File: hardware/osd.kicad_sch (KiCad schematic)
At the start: 17 parts, among them U18 SN74LVC1G3157DTBR, U19 TLV9061IDPWR, U20 TLV3201AIDBVR

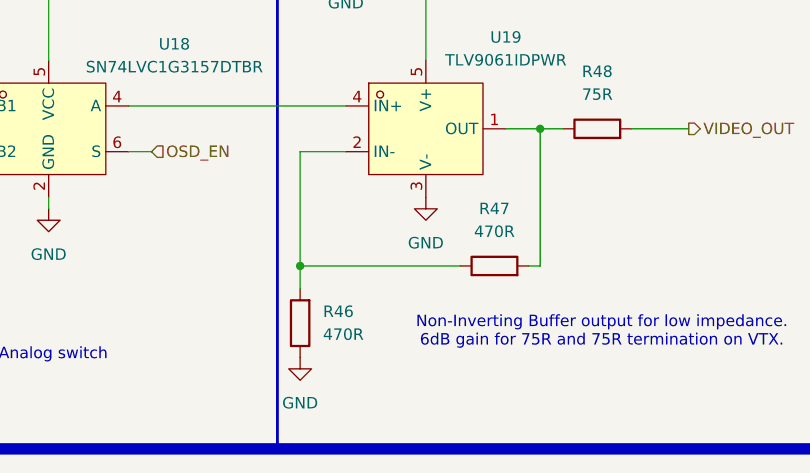
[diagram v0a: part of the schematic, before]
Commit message: LED resistors
Also reduced the amount of different resistors for cheaper assembly
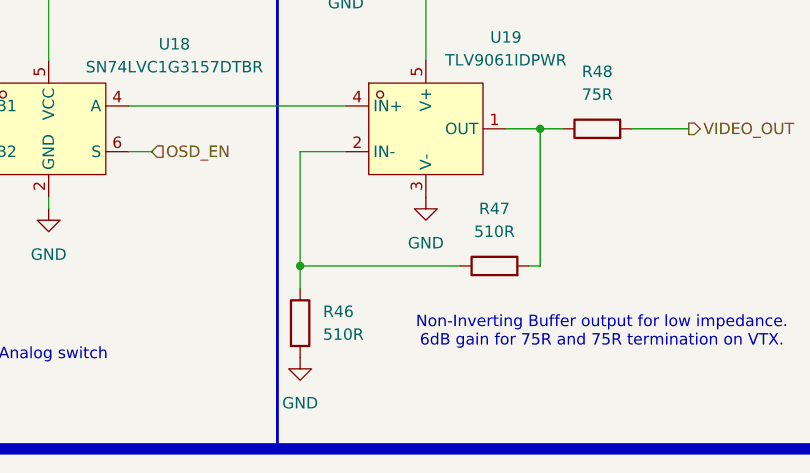
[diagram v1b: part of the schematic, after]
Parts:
- R46, R47: value 470R -> 510R; LCSC C473464 -> C57784; MPN 0201WMF4700TEE -> (none); Manufacturer UNI-ROYAL -> (none)
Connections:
- net GND: now also R46.2; no longer R46.1
- net at R47.1, U19.2 (IN-): now also R46.1; no longer R46.2
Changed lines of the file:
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@@
+	)
+	(symbol
+		(lib_id "Device:R")
+		(at 177.8 186.69 0)
+		(unit 1)
+		(body_style 1)
+		(exclude_from_sim no)
+		(in_bom yes)
+		(on_board yes)
+		(in_pos_files yes)
+		(dnp no)
+		(fields_autoplaced yes)
+		(property "Reference" "R46"
+			(at 180.34 185.4199 0)
+			(show_name no)
+			(do_not_autoplace no)
+			(effects
+				(font
+					(size 1.27 1.27)
+				)
+				(justify left)
+			)
+		)
+		(property "Value" "510R"
+			(at 180.34 187.9599 0)
+			(show_name no)
+			(do_not_autoplace no)
+			(effects
+				(font
+					(size 1.27 1.27)
+				)
+				(justify left)
+			)
+		)
+		(property "Footprint" "Resistor_SMD:R_0201_0603Metric"
+			(at 176.022 186.69 90)
+			(hide yes)
+			(show_name no)
+			(do_not_autoplace no)
+			(effects
+				(font
+					(size 1.27 1.27)
+				)
+			)
+		)
+		(property "Datasheet" ""
+			(at 177.8 186.69 0)
+			(hide yes)
+			(show_name no)
+			(do_not_autoplace no)
+			(effects
+				(font
+					(size 1.27 1.27)
+				)
+			)
+		)
+		(property "Description" "Resistor"
+			(at 177.8 186.69 0)
+			(hide yes)
+			(show_name no)
+			(do_not_autoplace no)
+			(effects
+				(font
+					(size 1.27 1.27)
+				)
+			)
+		)
+		(property "LCSC" "C57784"
+			(at 177.8 186.69 0)
+			(hide yes)
+			(show_name no)
+			(do_not_autoplace no)
+			(effects
+				(font
+					(size 1.27 1.27)
+				)
+			)
+		)
+		(property "MPN" ""
+			(at -74.93 82.55 0)
+			(hide yes)
+			(show_name no)
+			(do_not_autoplace no)
+			(effects
+				(font
+					(size 1.27 1.27)
+				)
+			)
+		)
+		(property "Manufacturer" ""
+			(at -74.93 82.55 0)
+			(hide yes)
+			(show_name no)
+			(do_not_autoplace no)
+			(effects
+				(font
+					(size 1.27 1.27)
+				)
+			)
+		)
+		(pin "1"
+		)
+		(pin "2"
+		)
+		(instances
+			(project "OpenFC"
+				(path "/fb88b6f9-ee39-4640-a9d4-04a17ceeac64/cd9508c6-33b2-4092-8e87-ecfbafcee27b"
+					(reference "R46")
+					(unit 1)
+				)
+			)
+		)
 	)
 	(symbol
@@
 	)
 	(symbol
-		(lib_id "Device:R")
-		(at 177.8 186.69 180)
-		(unit 1)
-		(body_style 1)
-		(exclude_from_sim no)
-		(in_bom yes)
-		(on_board yes)
-		(in_pos_files yes)
-		(dnp no)
-		(fields_autoplaced yes)
-		(property "Reference" "R46"
-			(at 180.34 185.4199 0)
-			(show_name no)
-			(do_not_autoplace no)
-			(effects
-				(font
-					(size 1.27 1.27)
-				)
-				(justify right)
-			)
-		)
-		(property "Value" "470R"
-			(at 180.34 187.9599 0)
-			(show_name no)
-			(do_not_autoplace no)
-			(effects
-				(font
-					(size 1.27 1.27)
-				)
-				(justify right)
-			)
-		)
-		(property "Footprint" "Resistor_SMD:R_0201_0603Metric"
-			(at 179.578 186.69 90)
-			(hide yes)
-			(show_name no)
-			(do_not_autoplace no)
-			(effects
-				(font
-					(size 1.27 1.27)
-				)
-			)
-		)
-		(property "Datasheet" ""
-			(at 177.8 186.69 0)
-			(hide yes)
-			(show_name no)
-			(do_not_autoplace no)
-			(effects
-				(font
-					(size 1.27 1.27)
-				)
-			)
-		)
-		(property "Description" "Resistor"
-			(at 177.8 186.69 0)
-			(hide yes)
-			(show_name no)
-			(do_not_autoplace no)
-			(effects
-				(font
-					(size 1.27 1.27)
-				)
-			)
-		)
-		(property "LCSC" "C473464"
-			(at 177.8 186.69 0)
-			(hide yes)
-			(show_name no)
-			(do_not_autoplace no)
-			(effects
-				(font
-					(size 1.27 1.27)
-				)
-			)
-		)
-		(property "MPN" "0201WMF4700TEE"
-			(at 0 0 0)
-			(hide yes)
-			(show_name no)
-			(do_not_autoplace no)
-			(effects
-				(font
-					(size 1.27 1.27)
-				)
-			)
-		)
-		(property "Manufacturer" "UNI-ROYAL"
-			(at 0 0 0)
-			(hide yes)
-			(show_name no)
-			(do_not_autoplace no)
-			(effects
-				(font
-					(size 1.27 1.27)
-				)
-			)
-		)
-		(pin "1"
-		)
-		(pin "2"
-		)
-		(instances
-			(project "OpenFC"
-				(path "/fb88b6f9-ee39-4640-a9d4-04a17ceeac64/cd9508c6-33b2-4092-8e87-ecfbafcee27b"
-					(reference "R46")
-					(unit 1)
-				)
-			)
-		)
-	)
-	(symbol
 		(lib_id "power:GND")
 		(at 168.91 119.38 0)
@@
 	)
 	(symbol
+		(lib_id "Device:R")
+		(at 199.39 180.34 90)
+		(unit 1)
+		(body_style 1)
+		(exclude_from_sim no)
+		(in_bom yes)
+		(on_board yes)
+		(in_pos_files yes)
+		(dnp no)
+		(fields_autoplaced yes)
+		(property "Reference" "R47"
+			(at 199.39 173.99 90)
+			(show_name no)
+			(do_not_autoplace no)
+			(effects
+				(font
+					(size 1.27 1.27)
+				)
+			)
+		)
+		(property "Value" "510R"
+			(at 199.39 176.53 90)
+			(show_name no)
+			(do_not_autoplace no)
+			(effects
+				(font
+					(size 1.27 1.27)
+				)
+			)
+		)
+		(property "Footprint" "Resistor_SMD:R_0201_0603Metric"
+			(at 199.39 182.118 90)
+			(hide yes)
+			(show_name no)
+			(do_not_autoplace no)
+			(effects
+				(font
+					(size 1.27 1.27)
+				)
+			)
+		)
+		(property "Datasheet" ""
+			(at 199.39 180.34 0)
+			(hide yes)
+			(show_name no)
+			(do_not_autoplace no)
+			(effects
+				(font
+					(size 1.27 1.27)
+				)
+			)
+		)
+		(property "Description" "Resistor"
+			(at 199.39 180.34 0)
+			(hide yes)
+			(show_name no)
+			(do_not_autoplace no)
+			(effects
+				(font
+					(size 1.27 1.27)
+				)
+			)
+		)
+		(property "LCSC" "C57784"
+			(at 199.39 180.34 0)
+			(hide yes)
+			(show_name no)
+			(do_not_autoplace no)
+			(effects
+				(font
+					(size 1.27 1.27)
+				)
+			)
+		)
+		(property "MPN" ""
+			(at 95.25 433.07 0)
+			(hide yes)
+			(show_name no)
+			(do_not_autoplace no)
+			(effects
+				(font
+					(size 1.27 1.27)
+				)
+			)
+		)
+		(property "Manufacturer" ""
+			(at 95.25 433.07 0)
+			(hide yes)
+			(show_name no)
+			(do_not_autoplace no)
+			(effects
+				(font
+					(size 1.27 1.27)
+				)
+			)
+		)
+		(pin "1"
+		)
+		(pin "2"
+		)
+		(instances
+			(project "OpenFC"
+				(path "/fb88b6f9-ee39-4640-a9d4-04a17ceeac64/cd9508c6-33b2-4092-8e87-ecfbafcee27b"
+					(reference "R47")
+					(unit 1)
+				)
+			)
+		)
+	)
+	(symbol
 		(lib_id "power:GND")
 		(at 191.77 172.72 0)
@@
 					(unit 1)
 				)
-			)
-		)
-	)
-	(symbol
-		(lib_id "Device:R")
-		(at 199.39 180.34 90)
-		(unit 1)
-		(body_style 1)
-		(exclude_from_sim no)
-		(in_bom yes)
-		(on_board yes)
-		(in_pos_files yes)
-		(dnp no)
-		(fields_autoplaced yes)
-		(property "Reference" "R47"
-			(at 199.39 173.99 90)
-			(show_name no)
-			(do_not_autoplace no)
-			(effects
-				(font
-					(size 1.27 1.27)
-				)
-			)
-		)
-		(property "Value" "470R"
-			(at 199.39 176.53 90)
-			(show_name no)
-			(do_not_autoplace no)
-			(effects
-				(font
-					(size 1.27 1.27)
-				)
-			)
-		)
-		(property "Footprint" "Resistor_SMD:R_0201_0603Metric"
-			(at 199.39 182.118 90)
-			(hide yes)
-			(show_name no)
-			(do_not_autoplace no)
-			(effects
-				(font
-					(size 1.27 1.27)
-				)
-			)
-		)
-		(property "Datasheet" ""
-			(at 199.39 180.34 0)
-			(hide yes)
-			(show_name no)
-			(do_not_autoplace no)
-			(effects
-				(font
-					(size 1.27 1.27)
-				)
-			)
-		)
-		(property "Description" "Resistor"
-			(at 199.39 180.34 0)
-			(hide yes)
-			(show_name no)
-			(do_not_autoplace no)
-			(effects
-				(font
-					(size 1.27 1.27)
-				)
-			)
-		)
-		(property "LCSC" "C473464"
-			(at 199.39 180.34 0)
-			(hide yes)
-			(show_name no)
-			(do_not_autoplace no)
-			(effects
-				(font
-					(size 1.27 1.27)
-				)
-			)
-		)
-		(property "MPN" "0201WMF4700TEE"
-			(at 0 0 0)
-			(hide yes)
-			(show_name no)
-			(do_not_autoplace no)
-			(effects
-				(font
-					(size 1.27 1.27)
-				)
-			)
-		)
-		(property "Manufacturer" "UNI-ROYAL"
-			(at 0 0 0)
-			(hide yes)
-			(show_name no)
-			(do_not_autoplace no)
-			(effects
-				(font
-					(size 1.27 1.27)
-				)
-			)
-		)
-		(pin "1"
-		)
-		(pin "2"
-		)
-		(instances
-			(project "OpenFC"
-				(path "/fb88b6f9-ee39-4640-a9d4-04a17ceeac64/cd9508c6-33b2-4092-8e87-ecfbafcee27b"
-					(reference "R47")
-					(unit 1)
-				)

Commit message: OSD
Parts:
- removed U19: TLV9061IDPWR, lib:X2SON-4_L0.8-W0.8-P0.48-TL-DPW, symbol lib:TLV9061IDPWR
- removed U20: TLV3201AIDBVR, lib:SOT-23-5_L3.0-W1.7-P0.95-LS2.8-BR, symbol lib:TLV3201AIDBVR
- added U1: COS8051SOT, lib:SOT-23-5_L3.0-W1.7-P0.95-LS2.8-BR, symbol lib:COS8051SOT
- added U2: TLV7031DPWR, lib:X2SON-4_L0.8-W0.8-P0.48-TL-A, symbol lib:TLV7031DPWR
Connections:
- net +3.3V: now also U1.5 (+VS), U2.2 (VCC)
- net GND: now also U1.2 (-VS), U2.3 (IN-), U2.5 (VEE)
- net OSD_SYNC: now also U2.1 (OUT)
- net VID_DC: now also U2.4 (IN+)
- net at R46.1, R47.1: now also U1.4 (IN-)
- net at R47.2, R48.1: now also U1.1 (OUT)
- net at U18.4 (A): now also U1.3 (IN+)
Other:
- moved on the sheet: R46, R47, R48
